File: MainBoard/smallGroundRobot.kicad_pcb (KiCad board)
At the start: 2 copper layers, 48.3 x 81.3 mm, 101 parts, among them CON1 AVR-JTAG-10, J101 Conn_01x03, J102 Conn_01x03, J105 USB_OTG, J505 Conn_01x03, J506 Conn_01x03, J507 Conn_01x03, J701 Screw_Terminal_01x02, M301 Motor_DC, M302 Motor_DC, M303 Motor_DC, M304 Motor_DC, Q501 Q_NPN_BEC, SW1 SW_SPDT, SW401 SW_SPDT, SW402 SW_SPDT, SW601 SW_DIP_x01, U1 ST8R00WPUR, U201 IMU, U202 Level_Shifter_4Channel, U301 A3916, U302 A3916, U504 OPB733TR, U601 STM32F303CCT6, U701 TPS62237, U702 TPS62231, U703 BQ2423, Y601 32.768kHz, Y602 8MHz

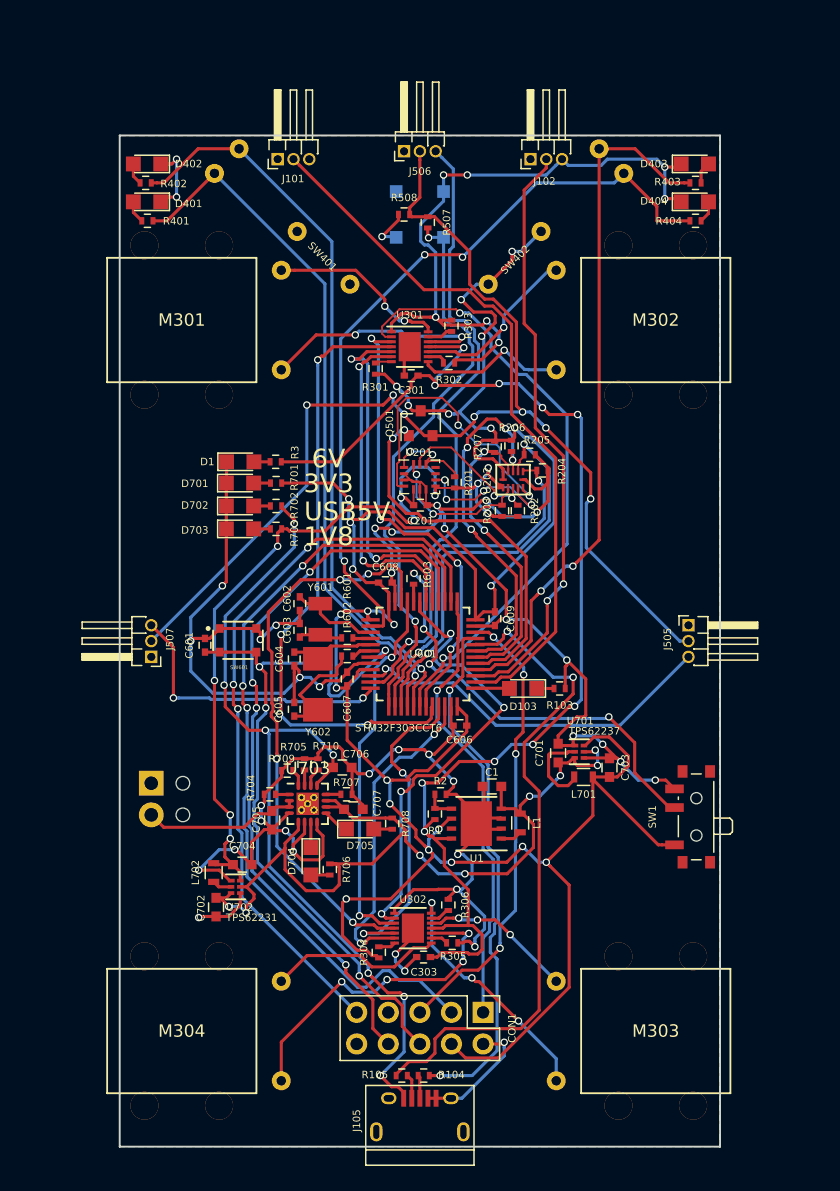
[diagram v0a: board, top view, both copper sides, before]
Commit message: Modified schematic for correct footprint
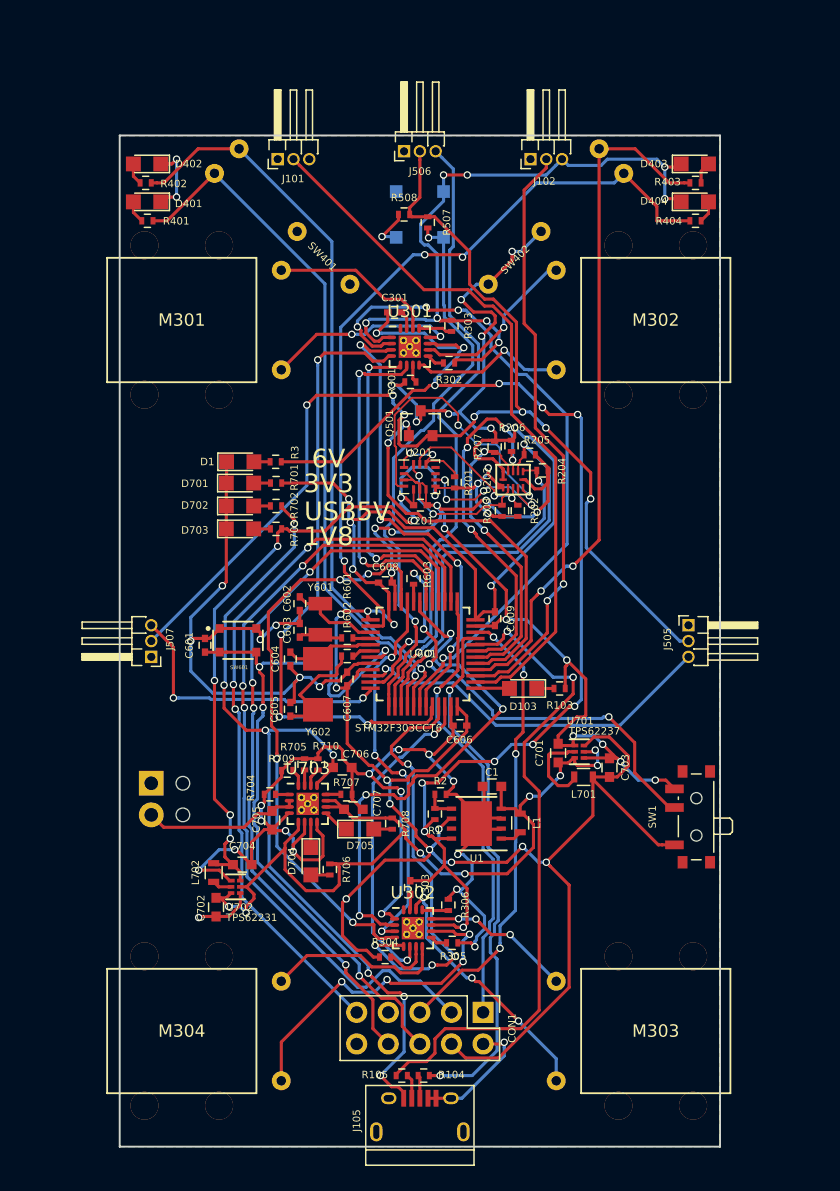
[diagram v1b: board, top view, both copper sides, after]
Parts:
- U301, U302: footprint Housings_DFN_QFN:DFN-14-1EP_3x3mm_Pitch0.4mm -> Housings_DFN_QFN:QFN-16-1EP_3x3mm_Pitch0.5mm_ThermalVias
- moved C303 5.69 mm to (147.8, 157.0), turned to 90 degrees
- moved C301 5.25 mm to (146.6, 110.7), turned to 180 degrees
- moved R301 2.99 mm to (147.8, 116.3), turned to 180 degrees
- moved R304 0.63 mm to (145.8, 162.6), turned to 180 degrees
- moved C604 0.32 mm to (138.2, 138.6)
- moved C605 0.32 mm to (138.2, 142.6)
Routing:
- net GND: track 304.6 -> 317.1 mm, vias 43 -> 46
- net /MC2_IN3: track 26.0 -> 34.9 mm, vias 2 -> 4
- net Net-(C303-Pad1): track 8.08 -> 1.26 mm, vias 2 -> 0
- net /MC2_SLEEPn: track 36.9 -> 41.6 mm
- net /MC1_SLEEPn: track 49.8 -> 54.4 mm, vias 2 -> 4
- net +6V: track 100.5 -> 104.9 mm, vias 10 -> 12
- net Net-(M301-Pad2): track 19.0 -> 15.6 mm
- net Net-(C301-Pad1): track 4.73 -> 1.46 mm
- net /MC1_IN3: track 28.5 -> 25.8 mm
- net /IRSensing/D_Power: track 96.2 -> 98.8 mm
- net Net-(R304-Pad1): track 1.39 -> 3.84 mm
- net /MC2_IN1: track 30.2 -> 31.4 mm, vias 2 -> 4
- net Net-(M301-Pad1): track 14.4 -> 13.3 mm, vias 2 -> 0
- net Net-(M303-Pad1): track 19.9 -> 20.8 mm
- net /MC1_IN1: track 37.1 -> 37.9 mm
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
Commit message: Modified design to have working 6V
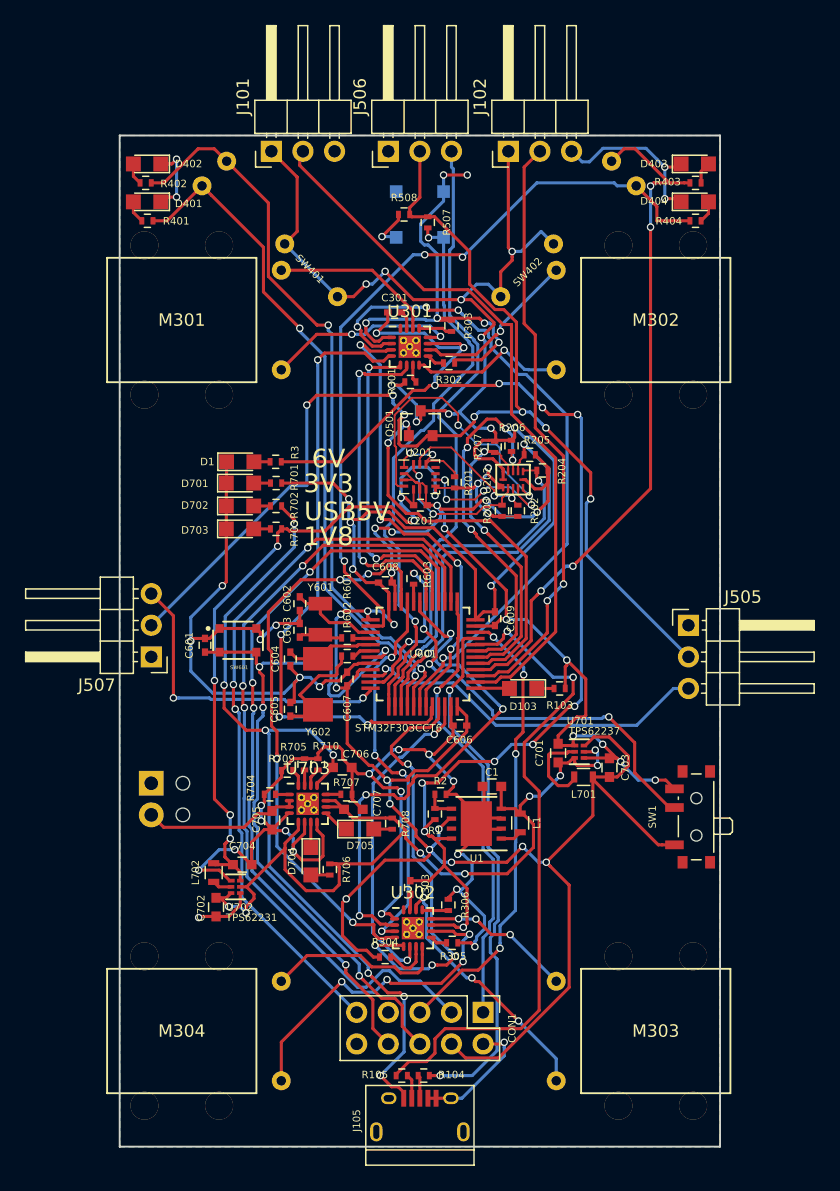
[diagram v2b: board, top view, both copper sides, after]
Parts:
- J101, J102, J505, J506, J507: footprint Pin_Headers:Pin_Header_Angled_1x03_Pitch1.27mm -> Pin_Headers:Pin_Header_Angled_1x03_Pitch2.54mm
- R1: value 10k -> 2.55k
- R2: value 2.55k -> 10k
- moved J102 1.89 mm to (155.7, 97.8)
- moved SW401 1.41 mm to (139.8, 107.4)
- moved SW402 1.41 mm to (157.2, 107.4)
- moved J506 1.27 mm to (146.1, 97.8)
- moved J101 0.81 mm to (136.7, 97.8)
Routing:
- net +3V3: track 219.0 -> 256.7 mm, vias 24 -> 26
- net GND: track 317.1 -> 309.0 mm
- net /Vout_IR_3: track 23.1 -> 25.6 mm
- net /T_FrontLeft: track 56.7 -> 54.7 mm, vias 1 -> 2
- net /Vout_IR_1: track 30.2 -> 29.1 mm
- net /IRSensing/D_Power: track 98.8 -> 99.8 mm
- net /T_BackLeft: track 60.0 -> 59.4 mm, vias 1 -> 2
- net /T_BackRight: track 62.1 -> 61.4 mm
- net /Vout_IR_2: track 50.5 -> 50.0 mm
- net /L1: track 57.3 -> 57.9 mm
- net /T_FrontRight: track 56.0 -> 55.7 mm, vias 2 -> 4
